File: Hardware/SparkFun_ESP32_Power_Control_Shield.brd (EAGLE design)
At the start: 101.6 x 50.8 mm, 68 parts, among them IC1 OP-AMP, IC2 OP-AMP, J2 POWER_JACKPTH_LOCK, U1 MC33926, U2 MC33926, U3 MC33926, U4 R-78E5.0-1.0

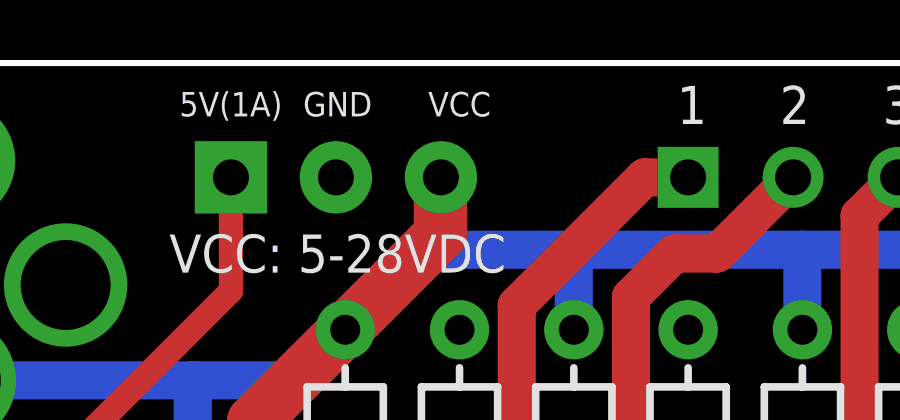
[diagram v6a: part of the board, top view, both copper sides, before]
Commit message: v10 changes additional
minor schematic layout changes, added values for the op-amps and diodes.
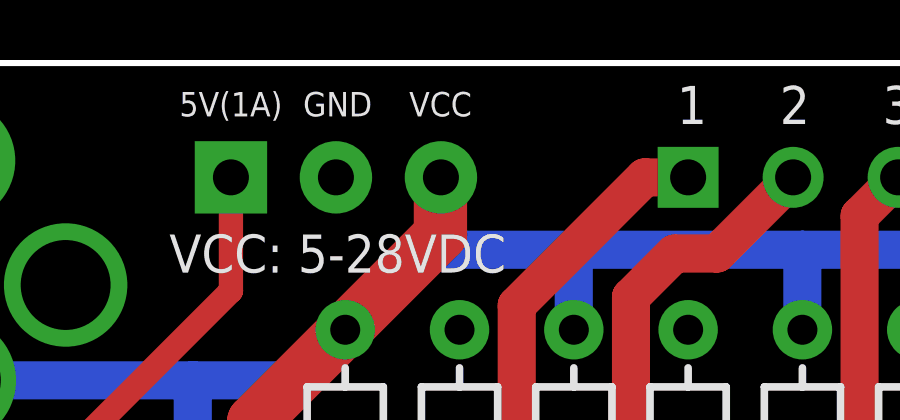
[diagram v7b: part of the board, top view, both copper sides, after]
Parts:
- D1, D10, D11, D12, D2, D3, D4, D5, D6, D7, D8, D9: value 1A/50V/1.1V -> 1N4001
- IC1, IC2: value OP-AMP -> LMV358
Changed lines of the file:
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@@
 <layer number="45" name="Holes" color="7" fill="1" visible="no" active="yes"/>
 <layer number="46" name="Milling" color="3" fill="1" visible="no" active="yes"/>
-<layer number="47" name="Measures" color="7" fill="1" visible="yes" active="yes"/>
+<layer number="47" name="Measures" color="7" fill="1" visible="no" active="yes"/>
 <layer number="48" name="Document" color="7" fill="1" visible="no" active="yes"/>
 <layer number="49" name="Reference" color="7" fill="1" visible="no" active="yes"/>
@@
 <text x="83.566" y="48.768" size="1.27" layer="21" font="vector" ratio="15" align="bottom-center">6</text>
 <text x="89.027" y="48.768" size="1.27" layer="21" font="vector" ratio="15" align="bottom-center">OUTPUT</text>
-<text x="58.42" y="49.022" size="0.8128" layer="21" font="vector" ratio="15" align="bottom-center">VCC</text>
+<text x="57.785" y="49.022" size="0.8128" layer="21" font="vector" ratio="15" align="bottom-center">VCC</text>
 <text x="54.356" y="49.022" size="0.8128" layer="21" font="vector" ratio="15" align="bottom-center">GND</text>
 <text x="54.356" y="43.815" size="1.27" layer="21" font="vector" ratio="15" align="bottom-center">VCC: 5-28VDC</text>
@@
 <text x="74.295" y="8.001" size="1.27" layer="21" font="vector" ratio="15" align="center-left">ESP32 Thing Power
 Control Shield</text>
-<wire x1="20.32" y1="50.165" x2="27.94" y2="50.165" width="0.254" layer="22"/>
-<wire x1="27.94" y1="50.165" x2="27.94" y2="46.609" width="0.254" layer="22"/>
-<wire x1="27.94" y1="46.609" x2="20.32" y2="46.609" width="0.254" layer="22"/>
-<wire x1="20.32" y1="46.609" x2="20.32" y2="50.165" width="0.254" layer="22"/>
-<text x="25.781" y="47.752" size="1.27" layer="22" font="vector" ratio="15" rot="MR0">USB</text>
-<wire x1="15.24" y1="50.165" x2="10.668" y2="50.165" width="0.254" layer="22"/>
-<wire x1="10.668" y1="50.165" x2="10.668" y2="43.688" width="0.254" layer="22"/>
-<wire x1="10.668" y1="43.688" x2="15.24" y2="43.688" width="0.254" layer="22"/>
-<wire x1="15.24" y1="43.688" x2="15.24" y2="50.165" width="0.254" layer="22"/>
-<text x="12.446" y="45.085" size="1.27" layer="22" font="vector" ratio="15" rot="MR90">BATT</text>
+<wire x1="11.43" y1="50.165" x2="19.05" y2="50.165" width="0.254" layer="22"/>
+<wire x1="19.05" y1="50.165" x2="19.05" y2="46.609" width="0.254" layer="22"/>
+<wire x1="19.05" y1="46.609" x2="11.43" y2="46.609" width="0.254" layer="22"/>
+<wire x1="11.43" y1="46.609" x2="11.43" y2="50.165" width="0.254" layer="22"/>
+<text x="16.891" y="47.752" size="1.27" layer="22" font="vector" ratio="15" rot="MR0">USB</text>
+<wire x1="29.21" y1="50.165" x2="24.638" y2="50.165" width="0.254" layer="22"/>
+<wire x1="24.638" y1="50.165" x2="24.638" y2="43.688" width="0.254" layer="22"/>
+<wire x1="24.638" y1="43.688" x2="29.21" y2="43.688" width="0.254" layer="22"/>
+<wire x1="29.21" y1="43.688" x2="29.21" y2="50.165" width="0.254" layer="22"/>
+<text x="26.416" y="45.085" size="1.27" layer="22" font="vector" ratio="15" rot="MR90">BATT</text>
 <text x="44.45" y="-22.86" size="1.778" layer="51" font="vector" ratio="15">Alex Wende</text>
 <dimension x1="98.425" y1="3.175" x2="101.6" y2="3.175" x3="100.0125" y3="-5.08" textsize="1.778" textratio="15" layer="47" unit="inch" precision="3"/>
@@
 <attribute name="PROD_ID" value="CAP-00868" x="50.038" y="18.542" size="1.778" layer="27" rot="R90" display="off"/>
 </element>
-<element name="D1" library="SparkFun-DiscreteSemi" package="DIODE-1N4001" value="1A/50V/1.1V" x="54.61" y="36.83" rot="R90">
+<element name="D1" library="SparkFun-DiscreteSemi" package="DIODE-1N4001" value="1N4001" x="54.61" y="36.83" rot="R90">
 <attribute name="PROD_ID" value="DIO-09176" x="54.61" y="36.83" size="1.778" layer="27" rot="R90" display="off"/>
 </element>
-<element name="D10" library="SparkFun-DiscreteSemi" package="DIODE-1N4001" value="1A/50V/1.1V" x="88.9" y="36.83" rot="R270">
+<element name="D10" library="SparkFun-DiscreteSemi" package="DIODE-1N4001" value="1N4001" x="88.9" y="36.83" rot="R270">
 <attribute name="PROD_ID" value="DIO-09176" x="88.9" y="36.83" size="1.778" layer="27" rot="R270" display="off"/>
 </element>
-<element name="D11" library="SparkFun-DiscreteSemi" package="DIODE-1N4001" value="1A/50V/1.1V" x="92.71" y="36.83" rot="R90">
+<element name="D11" library="SparkFun-DiscreteSemi" package="DIODE-1N4001" value="1N4001" x="92.71" y="36.83" rot="R90">
 <attribute name="PROD_ID" value="DIO-09176" x="92.71" y="36.83" size="1.778" layer="27" rot="R90" display="off"/>
 </element>
-<element name="D12" library="SparkFun-DiscreteSemi" package="DIODE-1N4001" value="1A/50V/1.1V" x="96.52" y="36.83" rot="R270">
+<element name="D12" library="SparkFun-DiscreteSemi" package="DIODE-1N4001" value="1N4001" x="96.52" y="36.83" rot="R270">
 <attribute name="PROD_ID" value="DIO-09176" x="96.52" y="36.83" size="1.778" layer="27" rot="R270" display="off"/>
 </element>
-<element name="D2" library="SparkFun-DiscreteSemi" package="DIODE-1N4001" value="1A/50V/1.1V" x="58.42" y="36.83" rot="R270">
+<element name="D2" library="SparkFun-DiscreteSemi" package="DIODE-1N4001" value="1N4001" x="58.42" y="36.83" rot="R270">
 <attribute name="PROD_ID" value="DIO-09176" x="58.42" y="36.83" size="1.778" layer="27" rot="R270" display="off"/>
 </element>
-<element name="D3" library="SparkFun-DiscreteSemi" package="DIODE-1N4001" value="1A/50V/1.1V" x="62.23" y="36.83" rot="R90">
+<element name="D3" library="SparkFun-DiscreteSemi" package="DIODE-1N4001" value="1N4001" x="62.23" y="36.83" rot="R90">
 <attribute name="PROD_ID" value="DIO-09176" x="62.23" y="36.83" size="1.778" layer="27" rot="R90" display="off"/>
 </element>
-<element name="D4" library="SparkFun-DiscreteSemi" package="DIODE-1N4001" value="1A/50V/1.1V" x="66.04" y="36.83" rot="R270">
+<element name="D4" library="SparkFun-DiscreteSemi" package="DIODE-1N4001" value="1N4001" x="66.04" y="36.83" rot="R270">
 <attribute name="PROD_ID" value="DIO-09176" x="66.04" y="36.83" size="1.778" layer="27" rot="R270" display="off"/>
 </element>
-<element name="D5" library="SparkFun-DiscreteSemi" package="DIODE-1N4001" value="1A/50V/1.1V" x="69.85" y="36.83" rot="R90">
+<element name="D5" library="SparkFun-DiscreteSemi" package="DIODE-1N4001" value="1N4001" x="69.85" y="36.83" rot="R90">
 <attribute name="PROD_ID" value="DIO-09176" x="69.85" y="36.83" size="1.778" layer="27" rot="R90" display="off"/>
 </element>
-<element name="D6" library="SparkFun-DiscreteSemi" package="DIODE-1N4001" value="1A/50V/1.1V" x="73.66" y="36.83" rot="R270">
+<element name="D6" library="SparkFun-DiscreteSemi" package="DIODE-1N4001" value="1N4001" x="73.66" y="36.83" rot="R270">
 <attribute name="PROD_ID" value="DIO-09176" x="73.66" y="36.83" size="1.778" layer="27" rot="R270" display="off"/>
 </element>
-<element name="D7" library="SparkFun-DiscreteSemi" package="DIODE-1N4001" value="1A/50V/1.1V" x="77.47" y="36.83" rot="R90">
+<element name="D7" library="SparkFun-DiscreteSemi" package="DIODE-1N4001" value="1N4001" x="77.47" y="36.83" rot="R90">
 <attribute name="PROD_ID" value="DIO-09176" x="77.47" y="36.83" size="1.778" layer="27" rot="R90" display="off"/>
 </element>
-<element name="D8" library="SparkFun-DiscreteSemi" package="DIODE-1N4001" value="1A/50V/1.1V" x="81.28" y="36.83" rot="R270">
+<element name="D8" library="SparkFun-DiscreteSemi" package="DIODE-1N4001" value="1N4001" x="81.28" y="36.83" rot="R270">
 <attribute name="PROD_ID" value="DIO-09176" x="81.28" y="36.83" size="1.778" layer="27" rot="R270" display="off"/>
 </element>
-<element name="D9" library="SparkFun-DiscreteSemi" package="DIODE-1N4001" value="1A/50V/1.1V" x="85.09" y="36.83" rot="R90">
+<element name="D9" library="SparkFun-DiscreteSemi" package="DIODE-1N4001" value="1N4001" x="85.09" y="36.83" rot="R90">
 <attribute name="PROD_ID" value="DIO-09176" x="85.09" y="36.83" size="1.778" layer="27" rot="R90" display="off"/>
 </element>
@@
 <attribute name="PROD_ID" value="CAP-08439" x="66.929" y="3.937" size="0.8128" layer="27" font="vector" ratio="15" rot="R90" display="off"/>
 </element>
-<element name="IC1" library="SparkFun-IC-Amplifiers" package="SO08" value="OP-AMP" x="47.752" y="12.192">
+<element name="IC1" library="SparkFun-IC-Amplifiers" package="SO08" value="LMV358" x="47.752" y="12.192">
 <attribute name="PROD_ID" value="IC-09657" x="47.752" y="12.192" size="0.8128" layer="27" font="vector" ratio="15" display="off"/>
 </element>
-<element name="IC2" library="SparkFun-IC-Amplifiers" package="SO08" value="OP-AMP" x="38.862" y="12.192">
+<element name="IC2" library="SparkFun-IC-Amplifiers" package="SO08" value="LMV358" x="38.862" y="12.192">
 <attribute name="PROD_ID" value="IC-09657" x="38.862" y="12.192" size="0.8128" layer="27" font="vector" ratio="15" display="off"/>
 </element>
